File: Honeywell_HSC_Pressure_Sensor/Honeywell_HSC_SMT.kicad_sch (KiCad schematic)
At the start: 5 parts, among them J1 Conn_01x04

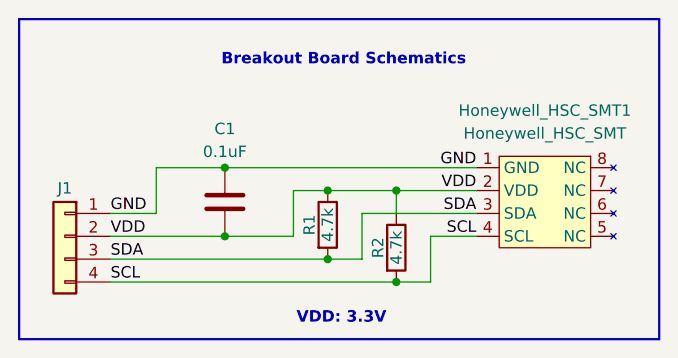
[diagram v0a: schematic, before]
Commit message: Honeywell_HSC_Pressure_Sensor break out board: changed 4.7kOhm to 10kOhm
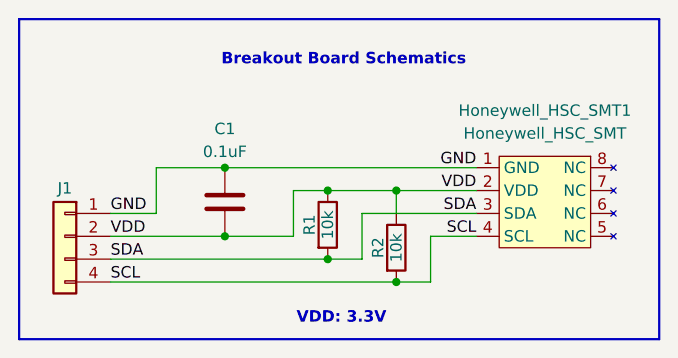
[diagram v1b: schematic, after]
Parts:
- R1, R2: value 4.7k -> 10k
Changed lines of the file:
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@@
 			)
 		)
-		(property "Value" "4.7k"
+		(property "Value" "10k"
 			(at 100.33 76.2 90)
 			(show_name no)
@@
 			)
 		)
-		(property "Value" "4.7k"
+		(property "Value" "10k"
 			(at 107.95 78.74 90)
 			(show_name no)
